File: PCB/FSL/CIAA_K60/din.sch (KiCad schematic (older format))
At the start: 53 parts, among them J701 DIG_INA, J702 DIG_INB, J703 DIG_INC, U701 PS2801-4, U702 PS2801-4

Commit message: Actualizacion de esquematicos. Circuito impreso y modelos 3D
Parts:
- removed D701, D702, D703, D704, D705, D706, D707, D708: LL4148, SOD-123, symbol DIODE
- removed D709, D710, D711, D712, D713, D714, D715, D716: P6SMB33CA, DO-214AA_SMB, symbol TVS
- removed U701, U702: PS2801-4, SSOP-16, symbol TLP291-4
- added D701, D702, D703, D704, D705, D706, D707, D708: LED red, LED-0603, symbol LED
- added U701, U702: TLP290-4, SSOP-16, symbol TLP290-4
- C701, C702, C703, C704, C705, C706, C707, C708: value 100nF -> 1,5nF; Descripcion CAP CER 0.1UF 50V Y5V 0603 -> CAP CER 1500PF 50V 10% X7R 0603; Digikey/Mouser 311-1343-2-ND -> 399-1084-1-ND; Fabricante Yageo -> Kemet; Nro. parte CC0603ZRY5V9BB104 -> C0603C152K5RACTU
- R701, R702, R703, R704, R705, R706, R707, R708: value 5,6K -> 4,7K 1/4W; footprint r_0603 -> r_1206; Descripcion RES 5.6K OHM 1/10W 5% 0603 SMD -> RES 4.7K OHM 1/4W 5% 1206 SMD; Digikey/Mouser 311-5.6KGRTR-ND -> 311-4.7KERCT-ND; Footprint estandar 0603 -> 1206; Nro. parte RC0603JR-075K6L -> RC1206JR-074K7L
- R709, R710, R711, R712, R713, R714, R715, R716: value 10K -> 1K; Descripcion RES 10K OHM 1/10W 5% 0603 SMD -> RES 1.0K OHM 1/10W 5% 0603 SMD; Digikey/Mouser 311-10KGRCT-ND -> 311-1.0KGRCT-ND; Nro. parte RC0603JR-0710KL -> RC0603JR-071KL
- R717, R718, R719, R720, R721, R722, R723, R724: value 4,7K -> 33K; Descripcion RES 4.7K OHM 1/10W 5% 0603 SMD -> RES 33K OHM 1/10W 5% 0603 SMD; Digikey/Mouser 311-4.7KGRTR-ND -> 311-33KGRCT-ND; Nro. parte RC0603JR-074K7L -> RC0603JR-0733KL
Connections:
- wire segments 130 -> 124
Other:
- note added: "Anti-Rebote"
- note added: "VIN = 10V\nIf = 1,9 mA\nCTR = 100%\nPdin = 17 mW"
- note added: "VIN = 24V\nIf = 4.8 mA\nCTR = 100%\nPdin = 110 mW"
- note added: "VIN = 30V\nIf = 6.1 mA\nCTR = 100%\nPdin = 176 mW"
- note removed: "Anti-Rebote\n(limitador)"
- note removed: "Protección contra \ninversión de \npolaridad y \nsobretensión"
- note removed: "VIN = 10V\nIf = 0,9 mA\nCTR = 100%\nIc = 0,9mA\nPdin = 9 mW"
- note removed: "VIN = 24V\nIf = 2.3 mA\nCTR = 150%\nIc = 3.45 mA\nPdin = 55 mW"
- note removed: "VIN = 30V\nIf = 2.9 mA\nCTR = 150%\nIc = 4.35 mA\nPdin = 87 mW"
- moved on the sheet: C701, J701, J702, J703, R701

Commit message: - Actualizado PCB - Actualizado documentación - Agregado scripts complementarios de kicad.
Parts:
- U701, U702: Descripcion (none) -> OPTOISOLTR 2.5KV 4CH TRANS 16-SO; Digikey/Mouser (none) -> TLP290-4(TPETR-ND; Fabricante (none) -> Toshiba Semiconductor and Storage; Footprint estandar (none) -> 16-SOIC; Nro. parte (none) -> TLP290-4(TP,E; Path datasheet (none) -> ../datasheets/ic/TLP290-4.pdf
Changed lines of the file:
@@
 EESchema Schematic File Version 2
 LIBS:CIAAK60LIB
-LIBS:CIAA_K60-cache
 EELAYER 27 0
 EELAYER END
@@
 Sheet 7 13
 Title "CIAA Entradas Digitales"
-Date "4 jul 2014"
+Date "25 aug 2014"
 Rev "1.0"
 Comp "CIAA - COMPUTADORA INDUSTRIAL ABIERTA ARGENTINA. Versión FSL (Freescale K60)"
@@
 F 2 "SSOP-16" H 4236 1076 29  0001 C CNN
 F 3 "~" H 4400 1250 60  0000 C CNN
+F 4 "OPTOISOLTR 2.5KV 4CH TRANS 16-SO" H 4400 1250 60  0001 C CNN "Descripcion"
+F 5 "Toshiba Semiconductor and Storage" H 4400 1250 60  0001 C CNN "Fabricante"
+F 6 "TLP290-4(TP,E" H 4400 1250 60  0001 C CNN "Nro. parte"
+F 7 "../datasheets/ic/TLP290-4.pdf" H 4400 1250 60  0001 C CNN "Path datasheet"
+F 8 "TLP290-4(TPETR-ND" H 4400 1250 60  0001 C CNN "Digikey/Mouser"
+F 9 "16-SOIC" H 4400 1250 60  0001 C CNN "Footprint estandar"
 	1    4400 1250
 	1    0    0    -1
@@
 F 2 "SSOP-16" H 4236 1926 29  0001 C CNN
 F 3 "~" H 4400 2100 60  0000 C CNN
+F 4 "OPTOISOLTR 2.5KV 4CH TRANS 16-SO" H 4400 1250 60  0001 C CNN "Descripcion"
+F 5 "Toshiba Semiconductor and Storage" H 4400 1250 60  0001 C CNN "Fabricante"
+F 6 "TLP290-4(TP,E" H 4400 1250 60  0001 C CNN "Nro. parte"
+F 7 "../datasheets/ic/TLP290-4.pdf" H 4400 1250 60  0001 C CNN "Path datasheet"
+F 8 "TLP290-4(TPETR-ND" H 4400 1250 60  0001 C CNN "Digikey/Mouser"
+F 9 "16-SOIC" H 4400 1250 60  0001 C CNN "Footprint estandar"
 	2    4400 2100
 	1    0    0    -1
@@
 F 2 "SSOP-16" H 4236 2776 29  0001 C CNN
 F 3 "~" H 4400 2950 60  0000 C CNN
+F 4 "OPTOISOLTR 2.5KV 4CH TRANS 16-SO" H 4400 1250 60  0001 C CNN "Descripcion"
+F 5 "Toshiba Semiconductor and Storage" H 4400 1250 60  0001 C CNN "Fabricante"
+F 6 "TLP290-4(TP,E" H 4400 1250 60  0001 C CNN "Nro. parte"
+F 7 "../datasheets/ic/TLP290-4.pdf" H 4400 1250 60  0001 C CNN "Path datasheet"
+F 8 "TLP290-4(TPETR-ND" H 4400 1250 60  0001 C CNN "Digikey/Mouser"
+F 9 "16-SOIC" H 4400 1250 60  0001 C CNN "Footprint estandar"
 	3    4400 2950
 	1    0    0    -1
@@
 F 2 "SSOP-16" H 4236 3626 29  0001 C CNN
 F 3 "~" H 4400 3800 60  0000 C CNN
+F 4 "OPTOISOLTR 2.5KV 4CH TRANS 16-SO" H 4400 1250 60  0001 C CNN "Descripcion"
+F 5 "Toshiba Semiconductor and Storage" H 4400 1250 60  0001 C CNN "Fabricante"
+F 6 "TLP290-4(TP,E" H 4400 1250 60  0001 C CNN "Nro. parte"
+F 7 "../datasheets/ic/TLP290-4.pdf" H 4400 1250 60  0001 C CNN "Path datasheet"
+F 8 "TLP290-4(TPETR-ND" H 4400 1250 60  0001 C CNN "Digikey/Mouser"
+F 9 "16-SOIC" H 4400 1250 60  0001 C CNN "Footprint estandar"
 	4    4400 3800
 	1    0    0    -1
@@
 F 2 "SSOP-16" H 4236 4476 29  0001 C CNN
 F 3 "~" H 4400 4650 60  0000 C CNN
+F 4 "OPTOISOLTR 2.5KV 4CH TRANS 16-SO" H 4400 1250 60  0001 C CNN "Descripcion"
+F 5 "Toshiba Semiconductor and Storage" H 4400 1250 60  0001 C CNN "Fabricante"
+F 6 "TLP290-4(TP,E" H 4400 1250 60  0001 C CNN "Nro. parte"
+F 7 "../datasheets/ic/TLP290-4.pdf" H 4400 1250 60  0001 C CNN "Path datasheet"
+F 8 "TLP290-4(TPETR-ND" H 4400 1250 60  0001 C CNN "Digikey/Mouser"
+F 9 "16-SOIC" H 4400 1250 60  0001 C CNN "Footprint estandar"
 	1    4400 4650
 	1    0    0    -1
@@
 F 2 "SSOP-16" H 4236 5326 29  0001 C CNN
 F 3 "~" H 4400 5500 60  0000 C CNN
+F 4 "OPTOISOLTR 2.5KV 4CH TRANS 16-SO" H 4400 1250 60  0001 C CNN "Descripcion"
+F 5 "Toshiba Semiconductor and Storage" H 4400 1250 60  0001 C CNN "Fabricante"
+F 6 "TLP290-4(TP,E" H 4400 1250 60  0001 C CNN "Nro. parte"
+F 7 "../datasheets/ic/TLP290-4.pdf" H 4400 1250 60  0001 C CNN "Path datasheet"
+F 8 "TLP290-4(TPETR-ND" H 4400 1250 60  0001 C CNN "Digikey/Mouser"
+F 9 "16-SOIC" H 4400 1250 60  0001 C CNN "Footprint estandar"
 	2    4400 5500
 	1    0    0    -1
@@
 F 2 "SSOP-16" H 4236 6176 29  0001 C CNN
 F 3 "~" H 4400 6350 60  0000 C CNN
+F 4 "OPTOISOLTR 2.5KV 4CH TRANS 16-SO" H 4400 1250 60  0001 C CNN "Descripcion"
+F 5 "Toshiba Semiconductor and Storage" H 4400 1250 60  0001 C CNN "Fabricante"
+F 6 "TLP290-4(TP,E" H 4400 1250 60  0001 C CNN "Nro. parte"
+F 7 "../datasheets/ic/TLP290-4.pdf" H 4400 1250 60  0001 C CNN "Path datasheet"
+F 8 "TLP290-4(TPETR-ND" H 4400 1250 60  0001 C CNN "Digikey/Mouser"
+F 9 "16-SOIC" H 4400 1250 60  0001 C CNN "Footprint estandar"
 	3    4400 6350
 	1    0    0    -1
@@
 F 2 "SSOP-16" H 4236 7026 29  0001 C CNN
 F 3 "~" H 4400 7200 60  0000 C CNN
+F 4 "OPTOISOLTR 2.5KV 4CH TRANS 16-SO" H 4400 1250 60  0001 C CNN "Descripcion"
+F 5 "Toshiba Semiconductor and Storage" H 4400 1250 60  0001 C CNN "Fabricante"
+F 6 "TLP290-4(TP,E" H 4400 1250 60  0001 C CNN "Nro. parte"
+F 7 "../datasheets/ic/TLP290-4.pdf" H 4400 1250 60  0001 C CNN "Path datasheet"
+F 8 "TLP290-4(TPETR-ND" H 4400 1250 60  0001 C CNN "Digikey/Mouser"
+F 9 "16-SOIC" H 4400 1250 60  0001 C CNN "Footprint estandar"
 	4    4400 7200
 	1    0    0    -1

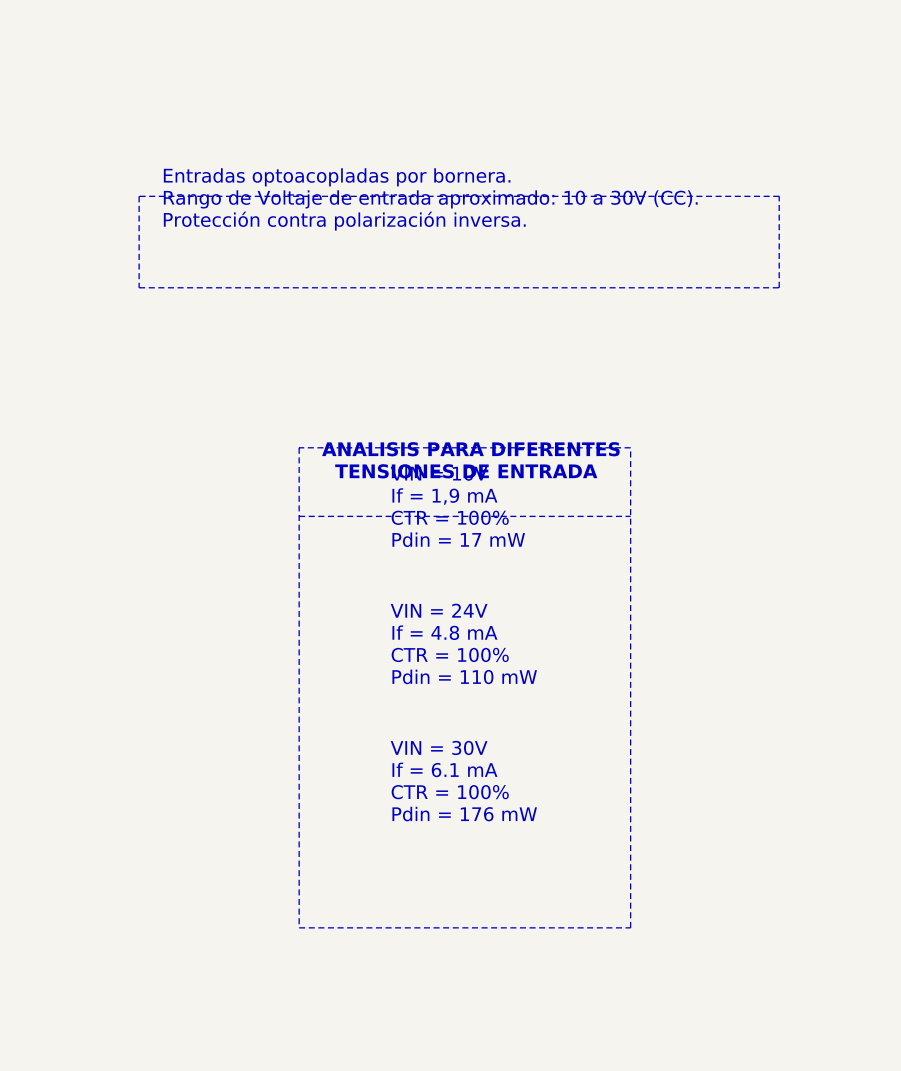
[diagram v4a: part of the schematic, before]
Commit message: Sch files adapted to new eeschema. Fixing some text locations.
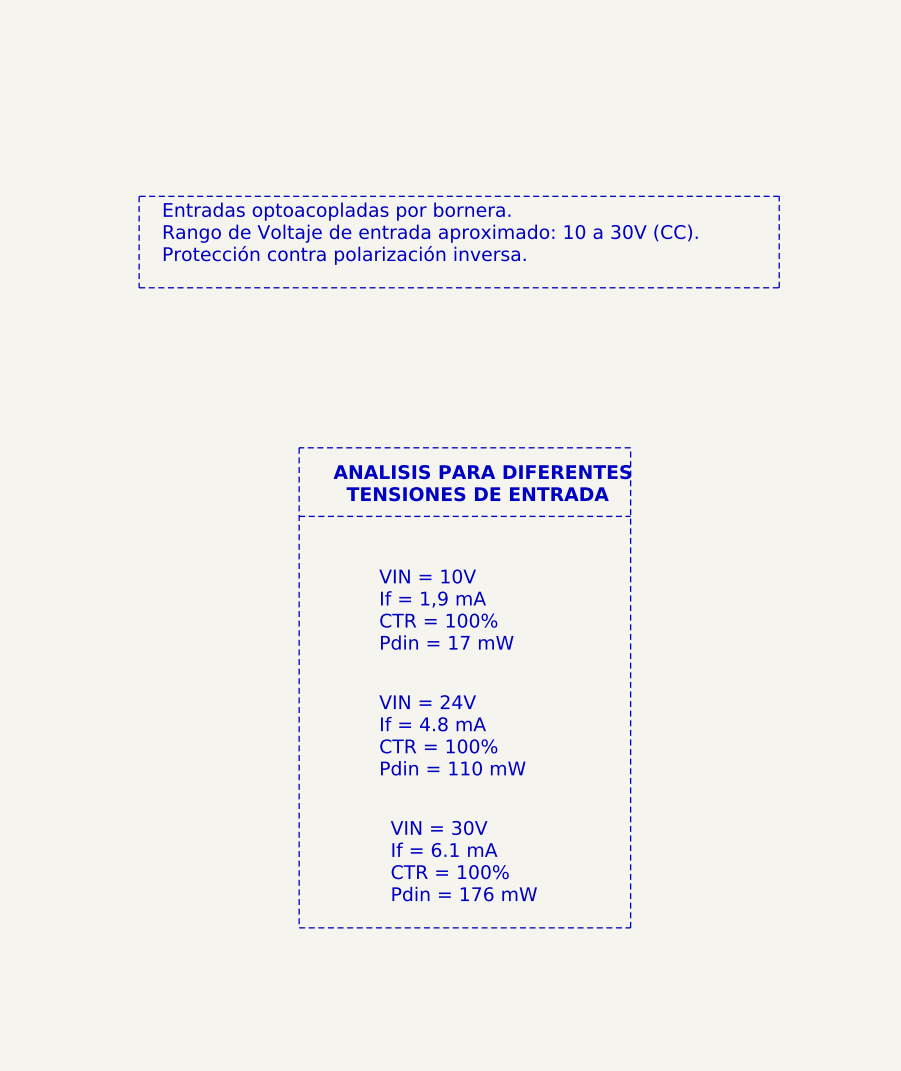
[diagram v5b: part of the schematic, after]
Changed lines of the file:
@@
 EESchema Schematic File Version 2
 LIBS:CIAAK60LIB
-EELAYER 27 0
+LIBS:CIAA_K60-cache
+EELAYER 25 0
 EELAYER END
 $Descr A4 11693 8268
@@
 Text Label 1650 4050 2    60   ~ 0
 IN6
-Text Notes 7850 1900 0    60   ~ 0
+Text Notes 7850 2050 0    60   ~ 0
 Entradas optoacopladas por bornera.\nRango de Voltaje de entrada aproximado: 10 a 30V (CC).\nProtección contra polarización inversa.
 $Comp
@@
 	0    -1   -1   0
 $EndComp
-Text Notes 8550 3000 0    60   ~ 12
+Text Notes 8600 3100 0    60   ~ 12
 ANALISIS PARA DIFERENTES\n  TENSIONES DE ENTRADA
-Text Notes 8850 3300 0    60   ~ 0
+Text Notes 8800 3750 0    60   ~ 0
 VIN = 10V\nIf = 1,9 mA\nCTR = 100%\nPdin = 17 mW
-Text Notes 8850 3900 0    60   ~ 0
+Text Notes 8800 4300 0    60   ~ 0
 VIN = 24V\nIf = 4.8 mA\nCTR = 100%\nPdin = 110 mW
-Text Notes 8850 4500 0    60   ~ 0
+Text Notes 8850 4850 0    60   ~ 0
 VIN = 30V\nIf = 6.1 mA\nCTR = 100%\nPdin = 176 mW
 Text Notes 600  750  0    120  ~ 24

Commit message: Renaming symbol field-names in .sch files for KiCost integration.
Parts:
- C701, C702, C703, C704, C705, C706, C707, C708: Desc (none) -> CAP CER 1500PF 50V 10% X7R 0603; Descripcion CAP CER 1500PF 50V 10% X7R 0603 -> (none); Digikey# (none) -> 399-1084-1-ND; Digikey/Mouser 399-1084-1-ND -> (none); Fabricante Kemet -> (none); Manf (none) -> Kemet; Manf# (none) -> C0603C152K5RACTU; Nro. parte C0603C152K5RACTU -> (none)
- D701, D702, D703, D704, D705, D706, D707, D708: Desc (none) -> LED ALG RED WTR CLR 0603 SMD; Descripcion LED ALG RED WTR CLR 0603 SMD -> (none); Digikey# (none) -> 1080-1400-1-ND; Digikey/Mouser 1080-1400-1-ND -> (none); Fabricante Everlight Electronics Co Ltd -> (none); Manf (none) -> Everlight Electronics Co Ltd; Manf# (none) -> QTLP600C7TR; Nro. parte QTLP600C7TR -> (none)
- J701, J702, J703: Desc (none) -> TERM BLOCK 5.08MM VERT 3POS PCB; Descripcion TERM BLOCK 5.08MM VERT 3POS PCB -> (none); Digikey# (none) -> 571-7969493; Digikey/Mouser 571-7969493 -> (none); Fabricante TE Connectivity -> (none); Manf (none) -> TE Connectivity; Manf# (none) -> 796949-3; Nro. parte 796949-3 -> (none)
- R701, R702, R703, R704, R705, R706, R707, R708: Desc (none) -> RES 4.7K OHM 1/4W 5% 1206 SMD; Descripcion RES 4.7K OHM 1/4W 5% 1206 SMD -> (none); Digikey# (none) -> 311-4.7KERCT-ND; Digikey/Mouser 311-4.7KERCT-ND -> (none); Fabricante Yageo -> (none); Manf (none) -> Yageo; Manf# (none) -> RC1206JR-074K7L; Nro. parte RC1206JR-074K7L -> (none)
- R709, R710, R711, R712, R713, R714, R715, R716: Desc (none) -> RES 1.0K OHM 1/10W 5% 0603 SMD; Descripcion RES 1.0K OHM 1/10W 5% 0603 SMD -> (none); Digikey# (none) -> 311-1.0KGRCT-ND; Digikey/Mouser 311-1.0KGRCT-ND -> (none); Fabricante Yageo -> (none); Manf (none) -> Yageo; Manf# (none) -> RC0603JR-071KL; Nro. parte RC0603JR-071KL -> (none)
- R717, R718, R719, R720, R721, R722, R723, R724: Desc (none) -> RES 33K OHM 1/10W 5% 0603 SMD; Descripcion RES 33K OHM 1/10W 5% 0603 SMD -> (none); Digikey# (none) -> 311-33KGRCT-ND; Digikey/Mouser 311-33KGRCT-ND -> (none); Fabricante Yageo -> (none); Manf (none) -> Yageo; Manf# (none) -> RC0603JR-0733KL; Nro. parte RC0603JR-0733KL -> (none)
- U701, U702: Desc (none) -> OPTOISOLTR 2.5KV 4CH TRANS 16-SO; Descripcion OPTOISOLTR 2.5KV 4CH TRANS 16-SO -> (none); Digikey# (none) -> TLP290-4(TPETR-ND; Digikey/Mouser TLP290-4(TPETR-ND -> (none); Fabricante Toshiba Semiconductor and Storage -> (none); Manf (none) -> Toshiba Semiconductor and Storage; Manf# (none) -> TLP290-4(TP,E; Nro. parte TLP290-4(TP,E -> (none)
